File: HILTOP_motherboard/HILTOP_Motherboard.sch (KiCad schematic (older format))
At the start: 202 parts, among them J1 BACKPLANE_PWR, J10 HDMI, J11 DISP_PWR, J12 DISPLAY_PORT, J14 VADJ_B, J15 VADJ_A, J16 SOFT_START_PWR, J17 PWR_LED, J18 USB_B, J19 Micro_SD_Card, J2 ATX_MOLEX_02X12, J20 CAMERA_PORT, J21 EXT_FAN, J22 BACKPLANE_LV_PWR, J23 EXT_FAN, J26 IO_EXP, J3 SATA, J4 USB_A_DOUBLE, J5 USB FRONT PANEL, J6 CAN, J7 RS485, J8 EXT_TEMP_MON, J9 RJ45-TRANS_SI-61001-F, U1 LM337BD2TG, U25 STM6719SFWB6F, U39 MCP23017

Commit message: finished new tracking for RS485 signals and general house keeping
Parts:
- added C53: 47pF, Capacitor_SMD:C_0603_1608Metric, symbol device:C
- added C55: 100nF, Capacitor_SMD:C_0603_1608Metric, symbol device:C
- added L12: 120R, 6A, Resistor_SMD:R_1206_3216Metric, symbol device:Ferrite_Bead
- added R206, R210, R213, R214: DNF, Resistor_SMD:R_0402_1005Metric, symbol device:R
- added R207, R211, R212, R250: 0R, Resistor_SMD:R_0402_1005Metric, symbol device:R
- added R93: 4K7, Resistor_SMD:R_0603_1608Metric, symbol device:R
- added U42: 24LC512, Package_SO:SOIC-8_3.9x4.9mm_P1.27mm, symbol memory:24LC512
- R148: value 330R -> 0R
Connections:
- wire segments 1032 -> 1077
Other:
- note added: "EEPROM"
- moved on the sheet: TP35, TP36, TP37, TP40, TP41, TP42

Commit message: Replaced FCC 15way connectors with new footprint
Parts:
- J12, J20: footprint Devtank_PCB_Lib:DSI_FCC15W_VERT -> Devtank_PCB_Lib:DSI_TE_1-1734248-5; Devtank 702-003 -> 702-004
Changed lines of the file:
@@
 EESchema Schematic File Version 4
 LIBS:HILTOP_Motherboard-cache
-EELAYER 26 0
+EELAYER 29 0
 EELAYER END
 $Descr A2 23386 16535
@@
 F 0 "J12" H 22150 11650 50  0000 C CNN
 F 1 "DISPLAY_PORT" V 22250 10850 50  0000 C CNN
-F 2 "Devtank_PCB_Lib:DSI_FCC15W_VERT" H 22150 10850 50  0001 C CNN
+F 2 "Devtank_PCB_Lib:DSI_TE_1-1734248-5" H 22150 10850 50  0001 C CNN
 F 3 "" H 22150 10850 50  0000 C CNN
-F 4 "702-003" H 22150 10850 60  0001 C CNN "Devtank"
+F 4 "702-004" H 22150 10850 60  0001 C CNN "Devtank"
 	1    22150 10850
 	1    0    0    -1
@@
 F 0 "J20" H 22150 14150 50  0000 C CNN
 F 1 "CAMERA_PORT" V 22250 13350 50  0000 C CNN
-F 2 "Devtank_PCB_Lib:DSI_FCC15W_VERT" H 22150 13350 50  0001 C CNN
+F 2 "Devtank_PCB_Lib:DSI_TE_1-1734248-5" H 22150 13350 50  0001 C CNN
 F 3 "" H 22150 13350 50  0000 C CNN
-F 4 "702-003" H 22150 13350 60  0001 C CNN "Devtank"
+F 4 "702-004" H 22150 13350 60  0001 C CNN "Devtank"
 	1    22150 13350
 	1    0    0    -1

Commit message: Rev B
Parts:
- D95: Devtank (none) -> 134-001
- J21, J23: Devtank 710-013 -> 710-019
- R207, R211, R212, R250: Devtank (none) -> 101-506
- R93: Devtank 101-010 -> 101-009
- U42: Devtank (none) -> 129-005
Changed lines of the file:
@@
 F 2 "Connector_Molex:Molex_KK-254_AE-6410-04A_1x04_P2.54mm_Vertical" H 22400 8775 50  0001 C CNN
 F 3 "" H 22400 8775 50  0001 C CNN
-F 4 "710-013" H 22400 8775 50  0001 C CNN "Devtank"
+F 4 "710-019" H 22400 8775 50  0001 C CNN "Devtank"
 	1    22400 8775
 	1    0    0    -1
@@
 F 2 "Connector_Molex:Molex_KK-254_AE-6410-04A_1x04_P2.54mm_Vertical" H 22400 7800 50  0001 C CNN
 F 3 "" H 22400 7800 50  0001 C CNN
-F 4 "710-013" H 22400 7800 50  0001 C CNN "Devtank"
+F 4 "710-019" H 22400 7800 50  0001 C CNN "Devtank"
 	1    22400 7800
 	1    0    0    -1
@@
 F 2 "Package_TO_SOT_SMD:SOT-23" H 13700 10350 50  0001 C CNN
 F 3 "" H 13700 10600 50  0001 C CNN
+F 4 "134-001" H 13700 10500 50  0001 C CNN "Devtank"
 	2    13700 10500
 	0    1    1    0
@@
 F 2 "Resistor_SMD:R_0603_1608Metric" V 20730 9500 50  0001 C CNN
 F 3 "" H 20800 9500 50  0000 C CNN
-F 4 "101-010" H 20800 9500 60  0001 C CNN "Devtank"
+F 4 "101-009" H 20800 9500 60  0001 C CNN "Devtank"
 	1    20800 9500
 	1    0    0    -1
@@
 F 2 "Package_SO:SOIC-8_3.9x4.9mm_P1.27mm" H 16975 14950 50  0001 L CNN
 F 3 "http://ww1.microchip.com/downloads/en/DeviceDoc/21754M.pdf" H 16925 15100 50  0001 C CNN
+F 4 "129-005" H 16925 15200 50  0001 C CNN "Devtank"
 	1    16925 15200
 	1    0    0    -1
@@
 F 2 "Resistor_SMD:R_0402_1005Metric" V 15930 15575 50  0001 C CNN
 F 3 "" H 16000 15575 50  0000 C CNN
+F 4 "101-506" H 16000 15575 50  0001 C CNN "Devtank"
 	1    16000 15575
 	1    0    0    -1
@@
 F 2 "Resistor_SMD:R_0402_1005Metric" V 15680 15575 50  0001 C CNN
 F 3 "" H 15750 15575 50  0000 C CNN
+F 4 "101-506" H 15750 15575 50  0001 C CNN "Devtank"
 	1    15750 15575
 	1    0    0    -1
@@
 F 2 "Resistor_SMD:R_0402_1005Metric" V 16180 14850 50  0001 C CNN
 F 3 "" H 16250 14850 50  0000 C CNN
+F 4 "101-506" H 16250 14850 50  0001 C CNN "Devtank"
 	1    16250 14850
 	1    0    0    -1
@@
 F 2 "Resistor_SMD:R_0402_1005Metric" V 17730 15550 50  0001 C CNN
 F 3 "" H 17800 15550 50  0000 C CNN
+F 4 "101-506" H 17800 15550 50  0001 C CNN "Devtank"
 	1    17800 15550
 	1    0    0    -1

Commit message: Rev C - pre-release
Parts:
- removed C1: 100nF, Capacitor_SMD:C_1210_3225Metric, symbol device:C
- removed D96: BAV99, Package_TO_SOT_SMD:SOT-23, symbol Diode:BAV99
- removed R148: 0R, Resistor_SMD:R_1210_3225Metric, symbol device:R
- removed R149, R150, R151: DNF, Resistor_SMD:R_1210_3225Metric, symbol device:R
- removed R249: 220R, Resistor_SMD:R_0402_1005Metric, symbol device:R
- added C1, C243: 100nF, Capacitor_SMD:C_0603_1608Metric, symbol HILTOP_Motherboard-rescue:C-device
- added C241, C242: 100uF, Capacitor_SMD:CP_Elec_6.3x7.7, symbol HILTOP_Motherboard-rescue:CP-device
- added J27: USB_A, Devtank_PCB_Lib:USB_A_Vertical_Lumberg_2410_01, symbol Connector:USB_A
- added R148: 0R, Resistor_SMD:R_0603_1608Metric, symbol HILTOP_Motherboard-rescue:R-device
- added R149: DNF, Resistor_SMD:R_0603_1608Metric, symbol HILTOP_Motherboard-rescue:R-device
- added TP96: TP, TestPoint:TestPoint_THTPad_D1.0mm_Drill0.5mm, symbol HILTOP_Motherboard-rescue:TEST_1P
- added U46: CM1624, Package_SON:WSON-16_3.3x1.35_P0.4mm, symbol Devtank:CM1624
- C10, C11, C119, C120, C13, C16, C18, C2, C3, C4, C6, C7, C9: symbol device:CP -> HILTOP_Motherboard-rescue:CP-device
- C12, C121, C14, C15, C17, C19, C20, C22, C24, C25, C26, C27, C5, C50, C51, C53, C55, C74, C75, C77, C8: symbol device:C -> HILTOP_Motherboard-rescue:C-device
- D1: symbol device:LED -> HILTOP_Motherboard-rescue:LED-device
- D34, D35, D93, D94, D95: symbol Diode:BAV99 -> HILTOP_Motherboard-rescue:BAV99-Diode
- F1, F2, F3: symbol device:Polyfuse -> HILTOP_Motherboard-rescue:Polyfuse-device
- J1: symbol Connector:Conn_02x04_Top_Bottom -> HILTOP_Motherboard-rescue:Conn_02x04_Top_Bottom-Connector
- J14, J15: symbol Connector:Conn_01x02 -> HILTOP_Motherboard-rescue:Conn_01x02-Connector
- J19: symbol Connector:Micro_SD_Card -> HILTOP_Motherboard-rescue:Micro_SD_Card-Connector
- J21, J23: symbol Connector:Conn_01x04 -> HILTOP_Motherboard-rescue:Conn_01x04-Connector
- J22: symbol Connector:Conn_02x02_Top_Bottom -> HILTOP_Motherboard-rescue:Conn_02x02_Top_Bottom-Connector
- J26: symbol Connector:Conn_02x06_Odd_Even -> HILTOP_Motherboard-rescue:Conn_02x06_Odd_Even-Connector
- J3: symbol Connector:Conn_01x07 -> HILTOP_Motherboard-rescue:Conn_01x07-Connector
- J5: symbol Connector:Conn_01x08 -> HILTOP_Motherboard-rescue:Conn_01x08-Connector
- J6: symbol Connector:Conn_02x05_Odd_Even -> HILTOP_Motherboard-rescue:Conn_02x05_Odd_Even-Connector
- J7: symbol Connector:Conn_02x08_Odd_Even -> HILTOP_Motherboard-rescue:Conn_02x08_Odd_Even-Connector
- J8: symbol Connector:Conn_01x03 -> HILTOP_Motherboard-rescue:Conn_01x03-Connector
- L1, L2, L3, L8: symbol device:L_Core_Ferrite -> HILTOP_Motherboard-rescue:L_Core_Ferrite-device
- L12: symbol device:Ferrite_Bead -> HILTOP_Motherboard-rescue:Ferrite_Bead-device
- R1, R10, R11, R119, R12, R120, R121, R122, R124, R125, R14, R16, R17, R18, R19, R2, R206, R207, R210, R211, R212, R213, R214, R22, R23, R24, R245, R246, R247, R248, R25, R250, R3, R4, R5, R54, R56, R6, R7, R83, R85, R9, R93: symbol device:R -> HILTOP_Motherboard-rescue:R-device
- R8: value 590R -> 360R; symbol device:R -> HILTOP_Motherboard-rescue:R-device
- U1: symbol regul:LM337_TO263 -> HILTOP_Motherboard-rescue:LM337_TO263-regul
- U39: symbol microchip:MCP23S17 -> HILTOP_Motherboard-rescue:MCP23S17-microchip
- U42: symbol memory:24LC512 -> HILTOP_Motherboard-rescue:24LC512-memory
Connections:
- net labels added: AUX_USB_N, AUX_USB_P, AUX_USB_PWR, CLK, CMD, D0, D1, D2, D3, PWR_SW_CPU
- net labels removed: EXT_GPIO6, Earth
- wire segments 1077 -> 1097
- no-connect marks 15 -> 13
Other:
- note removed: "DIGITAL GROUND to CHASSIS GROUND\n0R Links to be placed close to each Mounting hole"
- moved on the sheet: J16, J4, TP10, TP32, TP8, TP9, TP94, U25

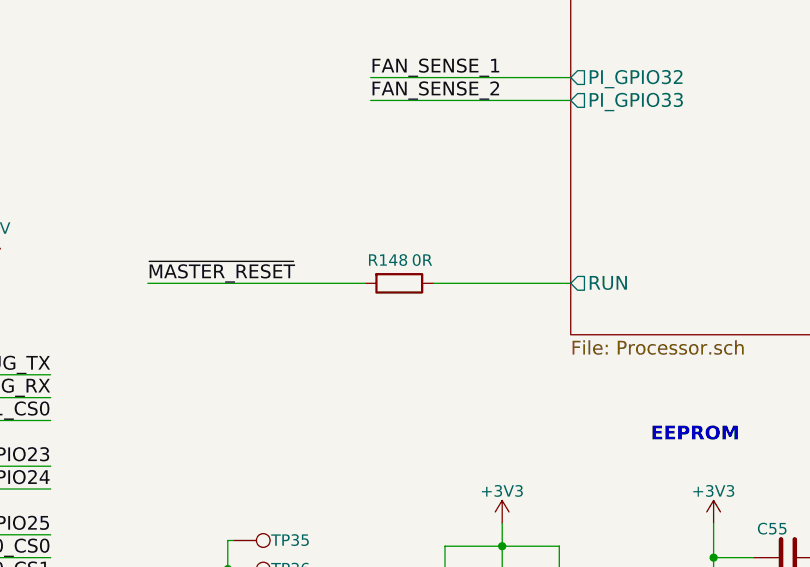
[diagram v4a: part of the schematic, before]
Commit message: Moved Backplane Connctor 2mm to the left to fix alignment issue on HILTOP 63HP
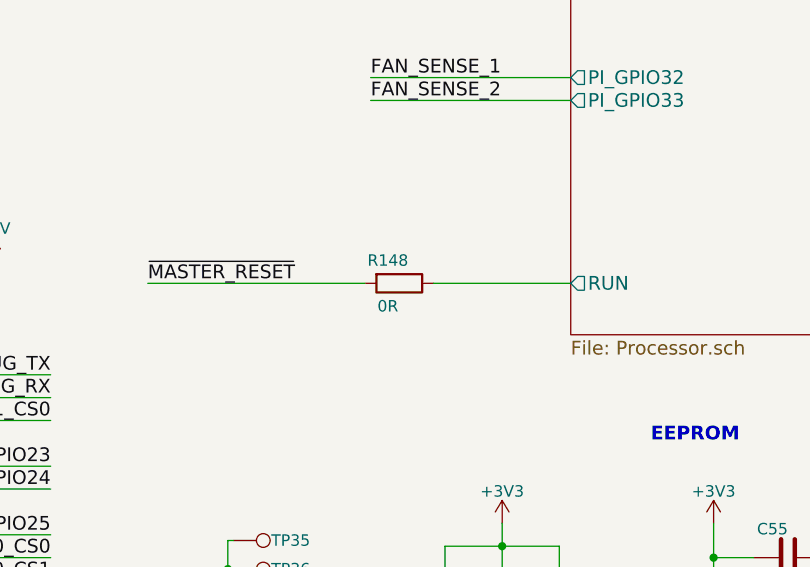
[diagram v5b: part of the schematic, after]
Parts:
- R8: Devtank 101-048 -> 101-
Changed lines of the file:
@@
 EESchema Schematic File Version 4
-LIBS:HILTOP_Motherboard-cache
-EELAYER 29 0
+EELAYER 30 0
 EELAYER END
 $Descr A2 23386 16535
@@
 Sheet 1 12
 Title "HILTOP Motherboard"
-Date "2019-07-03"
-Rev "Rev B"
+Date "2020-04-28"
+Rev "Rev C"
 Comp "Devtank Ltd"
 Comment1 ""
@@
 F 2 "Resistor_SMD:R_1206_3216Metric" V 5080 14350 50  0001 C CNN
 F 3 "" H 5150 14350 50  0000 C CNN
-F 4 "101-048" H 5150 14350 50  0001 C CNN "Devtank"
+F 4 "101-" H 5150 14350 50  0001 C CNN "Devtank"
 	1    5150 14350
 	1    0    0    -1
@@
 P 15550 13450
 F 0 "R148" V 15450 13400 50  0000 C CNN
-F 1 "0R" V 15450 13550 50  0000 C CNN
+F 1 "0R" V 15650 13400 50  0000 C CNN
 F 2 "Resistor_SMD:R_0603_1608Metric" V 15480 13450 50  0001 C CNN
 F 3 "" H 15550 13450 50  0000 C CNN
@@
 Connection ~ 7400 2450
 $Comp
-L power:GND #PWR?
+L power:GND #PWR0103
 U 1 1 60B25667
 P 6875 2500
-F 0 "#PWR?" H 6875 2250 50  0001 C CNN
+F 0 "#PWR0103" H 6875 2250 50  0001 C CNN
 F 1 "GND" H 6875 2350 50  0000 C CNN
 F 2 "" H 6875 2500 50  0000 C CNN
@@
 Connection ~ 6875 2100
 $Comp
-L power:GND #PWR?
+L power:GND #PWR0474
 U 1 1 61098A7A
 P 7850 3225
-F 0 "#PWR?" H 7850 2975 50  0001 C CNN
+F 0 "#PWR0474" H 7850 2975 50  0001 C CNN
 F 1 "GND" H 7850 3075 50  0000 C CNN
 F 2 "" H 7850 3225 50  0000 C CNN

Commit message: updates to include - license, remove U46, swap crystal Y1
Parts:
- removed C1: 100nF, Capacitor_SMD:C_0603_1608Metric, symbol HILTOP_Motherboard-rescue:C-device
- removed U46: CM1624, Package_SON:WSON-16_3.3x1.35_P0.4mm, symbol Devtank:CM1624
- added TP97: TP, TestPoint:TestPoint_THTPad_D1.0mm_Drill0.5mm, symbol HILTOP_Motherboard-rescue:TEST_1P
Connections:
- wire segments 1097 -> 1086
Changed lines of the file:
@@
 $EndComp
 Wire Wire Line
-	4450 8400 4650 8400
+	4450 8400 4525 8400
 Wire Wire Line
 	4650 8300 4650 8400
@@
 	1    0    0    -1
 $EndComp
-$Comp
-L Devtank:CM1624 U46
-U 1 1 5EBFC669
-P 19500 5875
-F 0 "U46" H 19500 6542 50  0000 C CNN
-F 1 "CM1624" H 19500 6451 50  0000 C CNN
-F 2 "Package_SON:WSON-16_3.3x1.35_P0.4mm" H 20600 6425 50  0001 C CNN
-F 3 "https://www.onsemi.com/pub/Collateral/CM1624-D.PDF" H 19100 6475 50  0001 C CNN
-	1    19500 5875
-	1    0    0    -1
-$EndComp
-$Comp
-L power:GND #PWR0471
-U 1 1 5F651B1E
-P 19500 6625
-F 0 "#PWR0471" H 19500 6375 50  0001 C CNN
-F 1 "GND" H 19500 6475 50  0000 C CNN
-F 2 "" H 19500 6625 50  0000 C CNN
-F 3 "" H 19500 6625 50  0000 C CNN
-	1    19500 6625
-	1    0    0    -1
-$EndComp
-Wire Wire Line
-	19500 6625 19500 6575
 Wire Wire Line
 	18700 5475 18200 5475
@@
 	18700 6175 18200 6175
 Wire Wire Line
-	20300 5475 20475 5475
-Wire Wire Line
 	21025 5550 20825 5550
 Wire Wire Line
@@
 Wire Wire Line
 	21025 5950 20825 5950
-Wire Wire Line
-	20300 5575 20475 5575
-Wire Wire Line
-	20300 5675 20475 5675
-Wire Wire Line
-	20300 5975 20475 5975
-Wire Wire Line
-	20300 6075 20475 6075
-Wire Wire Line
-	20300 6175 20475 6175
-Text Label 20475 6175 2    60   ~ 0
-D2
-Text Label 20475 6075 2    60   ~ 0
-D3
-Text Label 20475 5975 2    60   ~ 0
-CMD
-Text Label 20475 5675 2    60   ~ 0
-CLK
-Text Label 20475 5575 2    60   ~ 0
-D0
-Text Label 20475 5475 2    60   ~ 0
-D1
 Text Label 20825 6250 0    60   ~ 0
 D1
@@
 Text Label 20825 5550 0    60   ~ 0
 D2
-$Comp
-L power:+3V3 #PWR0472
-U 1 1 612EA248
-P 20575 4825
-F 0 "#PWR0472" H 20575 4675 50  0001 C CNN
-F 1 "+3V3" H 20575 4965 50  0000 C CNN
-F 2 "" H 20575 4825 50  0000 C CNN
-F 3 "" H 20575 4825 50  0000 C CNN
-	1    20575 4825
-	1    0    0    -1
-$EndComp
-Wire Wire Line
-	20575 4825 20575 5050
-Wire Wire Line
-	20300 5875 20575 5875
-$Comp
-L HILTOP_Motherboard-rescue:C-device C1
-U 1 1 6143B598
-P 20325 5050
-F 0 "C1" V 20225 4900 50  0000 L CNN
-F 1 "100nF" V 20225 5100 50  0000 L CNN
-F 2 "Capacitor_SMD:C_0603_1608Metric" H 20363 4900 50  0001 C CNN
-F 3 "" H 20325 5050 50  0000 C CNN
-F 4 "105-002" V 20325 5050 60  0001 C CNN "Devtank"
-	1    20325 5050
-	0    1    1    0
-$EndComp
-Wire Wire Line
-	20475 5050 20575 5050
-Connection ~ 20575 5050
-Wire Wire Line
-	20575 5050 20575 5875
-$Comp
-L power:GND #PWR0473
-U 1 1 6158BFF0
-P 20100 5150
-F 0 "#PWR0473" H 20100 4900 50  0001 C CNN
-F 1 "GND" H 20100 5000 50  0000 C CNN
-F 2 "" H 20100 5150 50  0000 C CNN
-F 3 "" H 20100 5150 50  0000 C CNN
-	1    20100 5150
-	1    0    0    -1
-$EndComp
-Wire Wire Line
-	20100 5150 20100 5050
-Wire Wire Line
-	20100 5050 20175 5050
 Wire Wire Line
 	16300 13450 15700 13450
@@
 Text Label 6525 3000 0    60   ~ 0
 AUX_USB_N
+Text Label 18625 6175 2    60   ~ 0
+D2
+Text Label 18625 6075 2    60   ~ 0
+D3
+Text Label 18600 5975 2    60   ~ 0
+CMD
+Text Label 18575 5675 2    60   ~ 0
+CLK
+Text Label 18550 5575 2    60   ~ 0
+D0
+Text Label 18550 5475 2    60   ~ 0
+D1
+$Comp
+L HILTOP_Motherboard-rescue:TEST_1P TP97
+U 1 1 607F2F10
+P 4525 8475
+F 0 "TP97" V 4525 8725 50  0000 C CNN
+F 1 "TP" H 4525 8675 50  0001 C CNN
+F 2 "TestPoint:TestPoint_THTPad_D1.0mm_Drill0.5mm" H 4725 8475 50  0001 C CNN
+F 3 "" H 4725 8475 50  0000 C CNN
+	1    4525 8475
+	-1   0    0    1
+$EndComp
+Wire Wire Line
+	4525 8475 4525 8400
+Connection ~ 4525 8400
+Wire Wire Line
+	4525 8400 4650 8400
 $EndSCHEMATC
